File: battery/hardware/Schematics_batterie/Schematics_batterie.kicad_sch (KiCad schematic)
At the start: 26 parts, among them IC1 BQ25185DLHR, J1 USB_C_Receptacle_USB2.0_16P, J3 Conn_01x02, J4 Conn_ST_STDC14, U1 BU33SD5WG-TR, U2 STM32G431KBTx, U3 USBLC6-2SC6

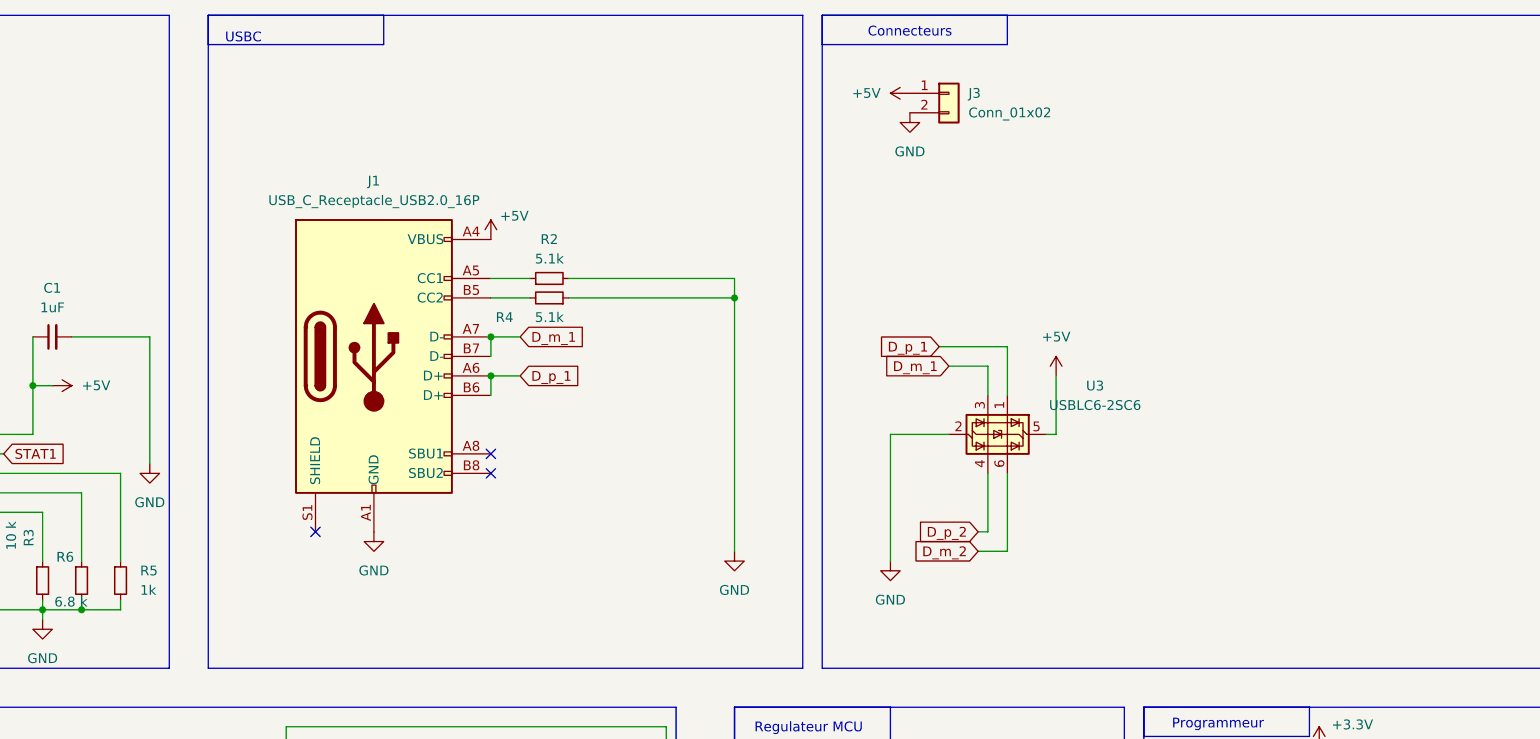
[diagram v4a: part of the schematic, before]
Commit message: ajout de footprint et début du PCB
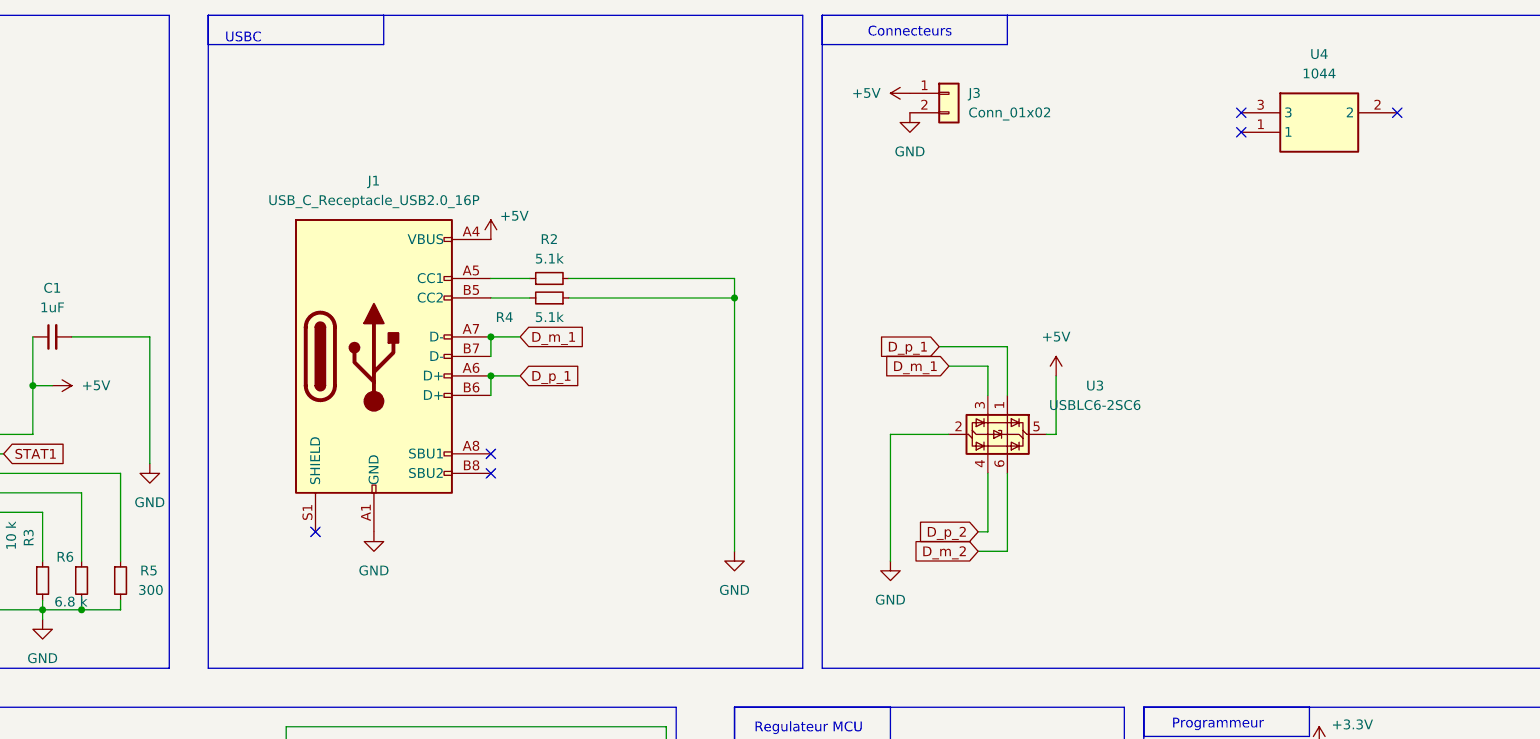
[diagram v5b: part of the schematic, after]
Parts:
- added U4: 1044, 1044, symbol 1044:1044
- C1, C11, C2, C3: footprint (none) -> Capacitor_SMD:C_0603_1608Metric_Pad1.08x0.95mm_HandSolder
- IC1: footprint (none) -> Package_SON:WSON-10-1EP_2.5x2.5mm_P0.5mm_EP1.2x2mm
- J4: footprint (none) -> Connector_PinHeader_1.27mm:PinHeader_2x07_P1.27mm_Vertical_SMD
- R2, R3, R4, R6: footprint (none) -> Resistor_SMD:R_0603_1608Metric_Pad0.98x0.95mm_HandSolder
- R5: value 1k -> 300; footprint (none) -> Resistor_SMD:R_0603_1608Metric_Pad0.98x0.95mm_HandSolder
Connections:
- no-connect marks 24 -> 27
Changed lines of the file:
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@@
 	)
 	(no_connect
+		(at 262.89 35.56)
+	)
+	(no_connect
 		(at 105.41 156.21)
 	)
 	(no_connect
+		(at 242.57 38.1)
+	)
+	(no_connect
 		(at 144.78 80.01)
 	)
@@
 	)
 	(no_connect
+		(at 242.57 35.56)
+	)
+	(no_connect
 		(at 130.81 161.29)
 	)
@@
 			)
 		)
-		(property "Footprint" ""
+		(property "Footprint" "Capacitor_SMD:C_0603_1608Metric_Pad1.08x0.95mm_HandSolder"
 			(at 100.33 143.51 0)
 			(effects
@@
 			)
 		)
-		(property "Footprint" ""
+		(property "Footprint" "Capacitor_SMD:C_0603_1608Metric_Pad1.08x0.95mm_HandSolder"
 			(at 87.63 64.77 0)
 			(effects
@@
 			)
 		)
-		(property "Footprint" ""
+		(property "Footprint" "Connector_PinHeader_1.27mm:PinHeader_2x07_P1.27mm_Vertical_SMD"
 			(at 252.73 135.89 0)
 			(effects
@@
 			)
 		)
-		(property "Footprint" ""
+		(property "Footprint" "Package_SON:WSON-10-1EP_2.5x2.5mm_P0.5mm_EP1.2x2mm"
 			(at 73.66 172.39 0)
 			(effects
@@
 			)
 		)
-		(property "Footprint" ""
+		(property "Footprint" "Capacitor_SMD:C_0603_1608Metric_Pad1.08x0.95mm_HandSolder"
 			(at 31.75 74.93 0)
 			(effects
@@
 			)
 		)
-		(property "Footprint" ""
+		(property "Footprint" "Resistor_SMD:R_0603_1608Metric_Pad0.98x0.95mm_HandSolder"
 			(at 152.4 59.69 0)
 			(effects
@@
 			)
 		)
-		(property "Footprint" ""
+		(property "Footprint" "Resistor_SMD:R_0603_1608Metric_Pad0.98x0.95mm_HandSolder"
 			(at 86.36 96.52 0)
 			(effects
@@
 			)
 		)
-		(property "Footprint" ""
+		(property "Footprint" "Capacitor_SMD:C_0603_1608Metric_Pad1.08x0.95mm_HandSolder"
 			(at 36.83 39.37 0)
 			(effects
@@
 		(on_board yes)
 		(dnp no)
-		(fields_autoplaced yes)
 		(property "Reference" "R5"
 			(at 99.06 95.2499 0)
@@
 			)
 		)
-		(property "Value" "1k"
-			(at 99.06 97.7899 0)
+		(property "Value" "300"
+			(at 98.806 97.79 0)
 			(effects
 				(font
@@
 			)
 		)
-		(property "Footprint" ""
+		(property "Footprint" "Resistor_SMD:R_0603_1608Metric_Pad0.98x0.95mm_HandSolder"
 			(at 96.52 96.52 0)
 			(effects
@@
 			)
 		)
-		(property "Footprint" ""
+		(property "Footprint" "Resistor_SMD:R_0603_1608Metric_Pad0.98x0.95mm_HandSolder"
 			(at 152.4 57.15 0)
 			(effects
@@
 			)
 		)
-		(property "Footprint" ""
+		(property "Footprint" "Resistor_SMD:R_0603_1608Metric_Pad0.98x0.95mm_HandSolder"
 			(at 91.44 96.52 0)
 			(effects
@@
 					(unit 1)
 				)
+			)
+		)
+	)
+	(symbol
+		(lib_id "1044:1044")
+		(at 242.57 35.56 0)
+		(unit 1)
+		(exclude_from_sim no)
+		(in_bom yes)
+		(on_board yes)
+		(dnp no)
+		(fields_autoplaced yes)
+		(property "Reference" "U4"
+			(at 252.73 27.94 0)
+			(effects
+				(font
+					(size 1.27 1.27)
+				)
+			)
+		)
+		(property "Value" "1044"
+			(at 252.73 30.48 0)
+			(effects
+				(font
+					(size 1.27 1.27)
+				)
+			)
+		)
+		(property "Footprint" "1044"
+			(at 259.08 130.48 0)
+			(effects
+				(font
+					(size 1.27 1.27)
+				)
+				(justify left top)
+				(hide yes)
+			)
+		)
+		(property "Datasheet" "http://www.keyelco.com/product-pdf.cfm?p=14060"
+			(at 259.08 230.48 0)
+			(effects
+				(font
+					(size 1.27 1.27)
+				)
+				(justify left top)
+				(hide yes)
+			)
+		)
+		(property "Description" "Cylindrical Battery Contacts, Clips, Holders & Springs 18650 SOLDER TAIL BATTERY HOLDER"
+			(at 242.57 35.56 0)
+			(effects
+				(font
+					(size 1.27 1.27)
+				)
+				(hide yes)
+			)
+		)
+		(property "Height" "14.86"
+			(at 259.08 430.48 0)
+			(effects
+				(font
+					(size 1.27 1.27)
+				)
+				(justify left top)
+				(hide yes)
+			)
+		)
+		(property "Mouser Part Number" "534-1044"
+			(at 259.08 530.48 0)
+			(effects
+				(font
+					(size 1.27 1.27)
+				)
+				(justify left top)
+				(hide yes)
+			)
+		)
+		(property "Mouser Price/Stock" "https://www.mouser.co.uk/ProductDetail/Keystone-Electronics/1044?qs=up89fPMRNqDbJ6cCmjKOVA%3D%3D"
+			(at 259.08 630.48 0)
+			(effects
+				(font
+					(size 1.27 1.27)
+				)
+				(justify left top)
+				(hide yes)
+			)
+		)
+		(property "Manufacturer_Name" "Keystone Electronics"
+			(at 259.08 730.48 0)
+			(effects
+				(font
+					(size 1.27 1.27)
+				)
+				(justify left top)
+				(hide yes)
+			)
+		)
+		(property "Manufacturer_Part_Number" "1044"
+			(at 259.08 830.48 0)
+			(effects
+				(font
+					(size 1.27 1.27)
+				)
+				(justify left top)
+				(hide yes)
+			)
+		)
+		(pin "3"
+		)
+		(pin "2"
+		)
+		(pin "1"
+		)
+		(instances
+			(project ""
+				(path "/4fbe78ef-b629-4e84-bfa0-c62113a81c93"
+					(reference "U4")
+					(unit 1)
+				)

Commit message: mise en place des étiquettes
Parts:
- removed U4: 1044, 1044, symbol 1044:1044
- added J2, J5: Conn_01x02, Connector_JST:JST_XH_B2B-XH-A_1x02_P2.50mm_Vertical, symbol Connector_Generic:Conn_01x02
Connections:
- net +5V: now also J2.1 (Pin_1)
- net BAT: now also J5.1 (Pin_1)
- net Charge Enabler: now also U2.9 (PA4)
- net GND: now also J2.2 (Pin_2), J5.2 (Pin_2)
- net STAT1: now also U2.10 (PA5)
- net STAT2: now also U2.11 (PA6)
- net SYS: now also U2.18 (PA8)
- no-connect marks 27 -> 20
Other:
- moved on the sheet: R1

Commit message: encore besoin de faire le rack a batterie
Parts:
- added D2: Green_LED, LED_SMD:LED_0603_1608Metric_Pad1.05x0.95mm_HandSolder, symbol Device:LED
- added R7: 1k, Resistor_SMD:R_0603_1608Metric_Pad0.98x0.95mm_HandSolder, symbol Device:R_Small
- R1: value 100 k -> 1k
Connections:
- net GND: now also R7.2
- net LED_Status: now also U2.18 (PA8); no longer U2.12 (PA7)
- net SYS: now also U2.12 (PA7); no longer U2.18 (PA8)
- net LED_Playing: now reaches U2.19 (PA9)
- net LED_Playing: now also D2.2 (A)
- new net: D2.1 (K), R7.1
- no-connect marks 20 -> 19
